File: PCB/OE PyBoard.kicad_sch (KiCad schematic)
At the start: 64 parts, among them J2 Micro_SD_Card, J3 USB4105-GF-A, J4 Conn_02x03_Odd_Even, J5 Conn_01x08, J6 Conn_01x08, J7 Conn_01x08, J8 Conn_01x08, J9 Conn_02x04_Odd_Even, U2 STM32F405RGT6, U3 MCP1700T, U4 FXLS8971CFR1, X2 12 MHz, X3 32.768 kHz

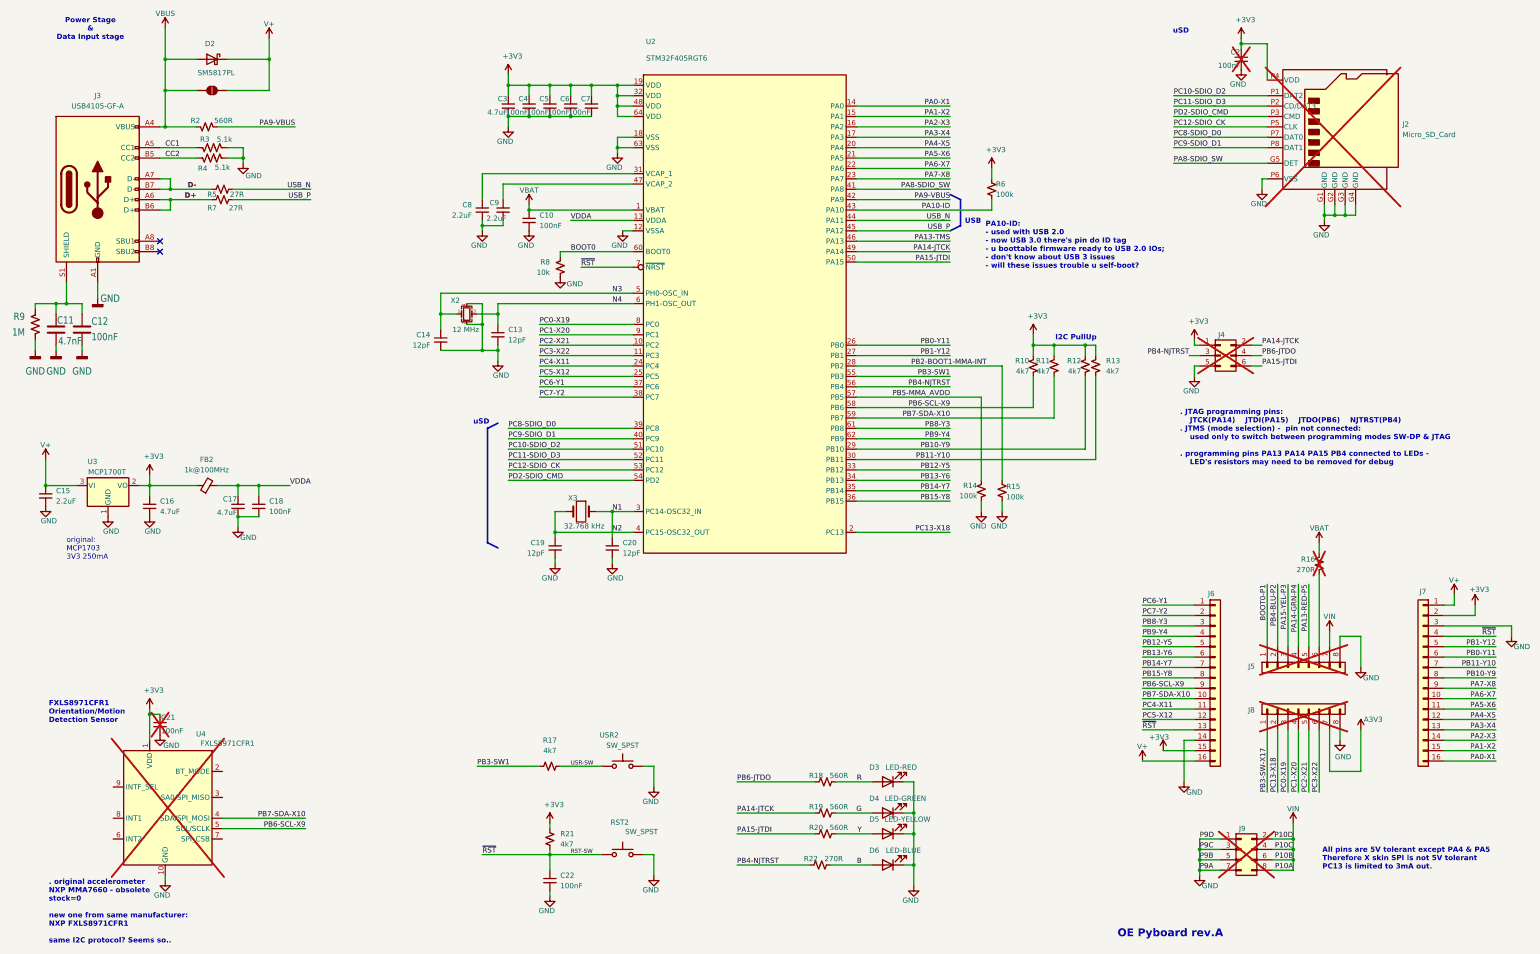
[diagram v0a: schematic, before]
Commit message: Fixed cristal and diode's footprint.
Also, updated the production files.

Co-Authored-By: David Palma <78764277+davidpalma666@users.noreply.github.com>
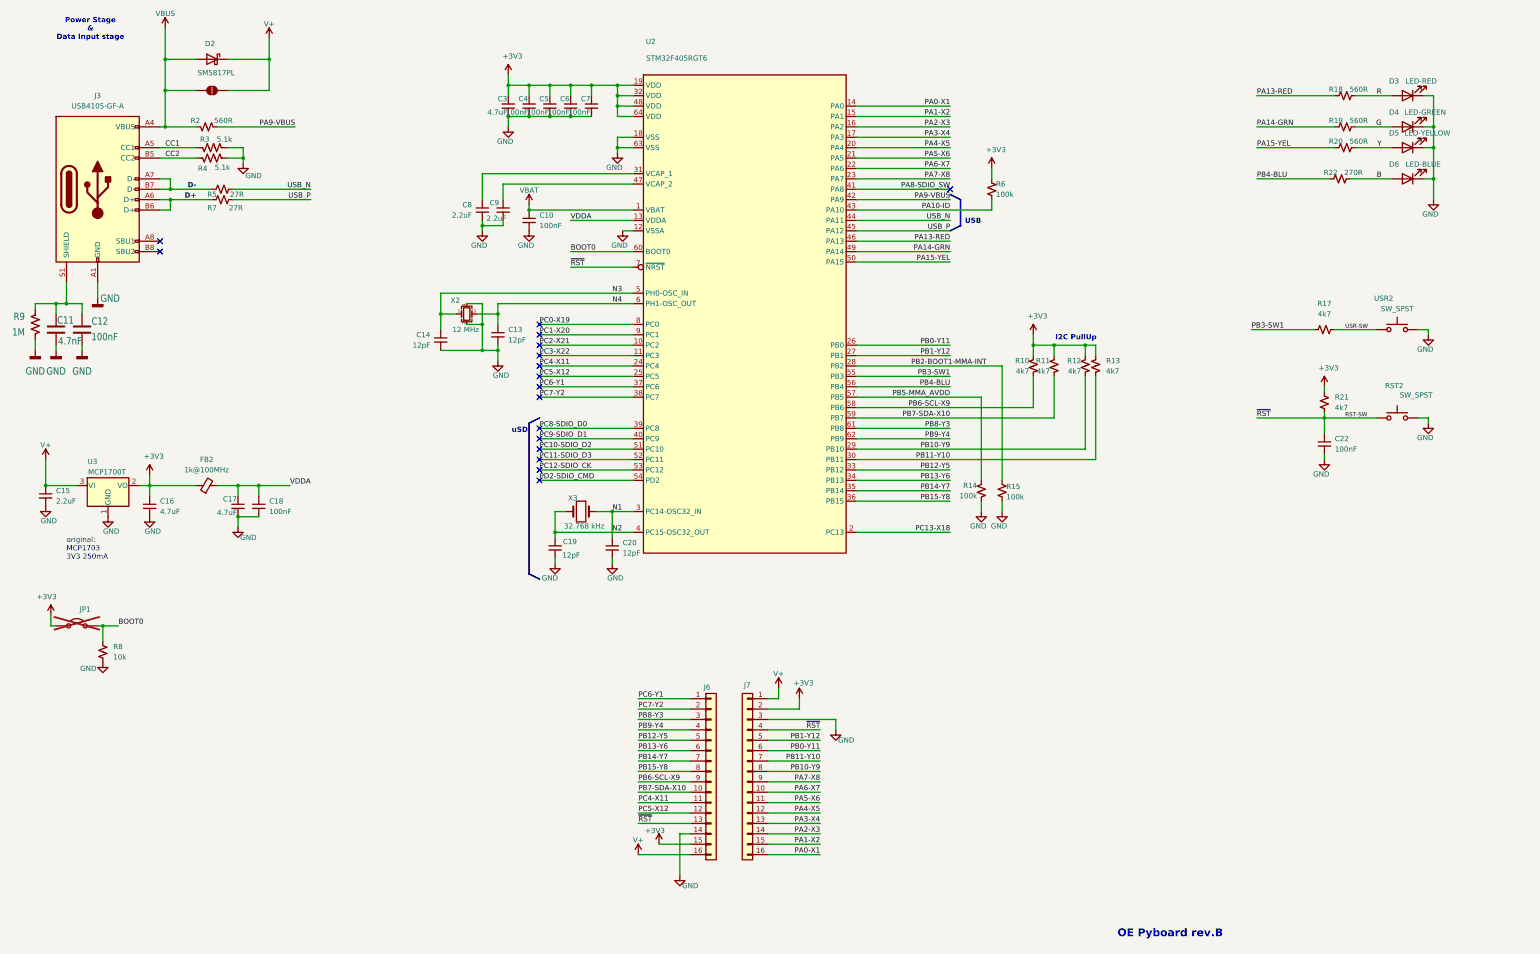
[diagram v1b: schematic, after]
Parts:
- removed C2, C21: 100nF, Capacitor_SMD:C_0402_1005Metric, symbol Device:C_Small
- removed J2: Micro_SD_Card, MicroPython FootprintLib:47571-0001_MOL, symbol PyBoard SymbLib:microSD Card
- removed J4: Conn_02x03_Odd_Even, Connector_PinSocket_2.54mm:PinSocket_2x03_P2.54mm_Vertical, symbol Connector_Generic:Conn_02x03_Odd_Even
- removed J5, J8: Conn_01x08, Connector_PinHeader_2.54mm:PinHeader_1x08_P2.54mm_Vertical, symbol Connector_Generic:Conn_01x08
- removed J9: Conn_02x04_Odd_Even, Connector_PinSocket_2.54mm:PinSocket_2x04_P2.54mm_Vertical, symbol Connector_Generic:Conn_02x04_Odd_Even
- removed R16: 270R, Resistor_SMD:R_0402_1005Metric, symbol Device:R_Small_US
- removed U4: FXLS8971CFR1, MicroPython FootprintLib:LQFN-12-3x3mm_P0.65mm, symbol MicroPython SymbLib:FXLS8971CFR1
- added JP1: Jumper, Connector_PinHeader_2.54mm:PinHeader_1x02_P2.54mm_Vertical, symbol Jumper:Jumper_2_Open
- D2: footprint Diode_SMD:D_SOD-128 -> Diode_SMD:D_SOD-123
- D3: MPN 5990010007F -> 5975004407F; OEPSPN OEPS030044 -> OEPS030006
- X2: footprint Crystal:Crystal_SMD_Abracon_ABM10-4Pin_2.5x2.0mm -> Crystal:Crystal_SMD_Abracon_ABM8AIG-4Pin_3.2x2.5mm
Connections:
- net PB6-JTDO is gone; now on net PA13-RED: R18.1
- net +3V3: now also JP1.2 (B)
- net BOOT0: now also JP1.1 (A)
- net PA13-TMS renamed PA13-RED
- net PA14-JTCK renamed PA14-GRN
- net PA15-JTDI renamed PA15-YEL
- net PB4-NJTRST renamed PB4-BLU
- no-connect marks 2 -> 17
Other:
- note added: "OE Pyboard rev.B"
- note removed: ". JTAG programming pins: JTCK(PA14) JTDI(PA15) JTDO(PB6) NJTRST(PB4) . JTMS (mode selection) - pin not connected: used only to switch between programming modes SW-DP & JTAG . programming pins PA13 PA14 PA15 PB4 connected to LEDs - LED's resistors may need to be removed for debug"
- note removed: ". original accelerometer NXP MMA7660 - obsolete stock=0 new one from same manufacturer: NXP FXLS8971CFR1 same I2C protocol? Seems so.."
- note removed: "All pins are 5V tolerant except PA4 & PA5 Therefore X skin SPI is not 5V tolerant PC13 is limited to 3mA out."
- note removed: "FXLS8971CFR1 Orientation/Motion Detection Sensor"
- note removed: "OE Pyboard rev.A"
- note removed: "PA10-ID: - used with USB 2.0 - now USB 3.0 there's pin do ID tag - u boottable firmware ready to USB 2.0 IOs; - don't know about USB 3 issues - will these issues trouble u self-boot?"
- moved on the sheet: C22, D3, D4, D5, D6, J6, J7, R17, R18, R19, R20, R21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

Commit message: Replaced D3 obsolete red LED in schematic, PCB, and BOM.
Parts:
- D3: MPN 5975004407F -> 5990010007F; OEPSPN OEPS030006 -> OEPS030044
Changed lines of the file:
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@@
 			)
 		)
-		(property "MPN" "5975004407F"
+		(property "MPN" "5990010007F"
 			(at 375.92 55.88 0)
 			(effects
@@
 			)
 		)
-		(property "OEPSPN" "OEPS030006"
+		(property "OEPSPN" "OEPS030044"
 			(at 375.92 55.88 0)
 			(effects
